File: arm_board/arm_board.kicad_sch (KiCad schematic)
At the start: 27 parts, among them J10 RJ45_LED_Shielded, Q3 BSS138, SW10 SW_Push, SW11 SW_Push, SW12 SW_Push, SW13 SW_Push, SW14 SW_Push, SW15 SW_SPDT, SW16 SW_SPDT, SW9 SW_Push

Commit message: Changed RX and TX on MCU
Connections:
- net RX+: now also U2.19 (RX+); no longer U2.20 (RX-)
- net RX-: now also U2.20 (RX-); no longer U2.19 (RX+)
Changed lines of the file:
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@@
-	(wire
-		(pts
-			(xy 67.31 167.64) (xy 71.12 167.64)
-		)
-		(stroke
-			(width 0)
-			(type default)
-		)
-	)
 	(wire
 		(pts
@@
 	(wire
 		(pts
-			(xy 67.31 170.18) (xy 71.12 170.18)
-		)
-		(stroke
-			(width 0)
-			(type default)
-		)
-	)
-	(wire
-		(pts
 			(xy 67.31 156.21) (xy 71.12 156.21)
 		)
@@
 	(wire
 		(pts
+			(xy 71.12 170.18) (xy 67.31 170.18)
+		)
+		(stroke
+			(width 0)
+			(type default)
+		)
+	)
+	(wire
+		(pts
 			(xy 33.02 168.91) (xy 43.18 168.91)
 		)
@@
 		(pts
 			(xy 229.87 137.16) (xy 238.76 137.16)
+		)
+		(stroke
+			(width 0)
+			(type default)
+		)
+	)
+	(wire
+		(pts
+			(xy 71.12 167.64) (xy 67.31 167.64)
 		)
 		(stroke
@@
 	)
 	(label "RX-"
+		(at 71.12 170.18 0)
+		(effects
+			(font
+				(size 1.27 1.27)
+			)
+			(justify left bottom)
+		)
+	)
+	(label "RX+"
 		(at 71.12 167.64 0)
 		(effects
 			(font
-				(size 1.27 1.27)
-			)
-			(justify left bottom)
-		)
-	)
-	(label "RX+"
-		(at 71.12 170.18 0)
-		(effects
-			(font

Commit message: I2C connector added
Also JST symbols added
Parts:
- removed Conn13, Conn14, Conn15, Conn16, Conn17: Molex_uF_S_03, MRDT_Connectors:MOLEX_uF_S_03_Horizontal, symbol MRDT_Connectors:Molex_uF_S_03
- removed Conn3, Conn5: Molex_uF_S_02, MRDT_Connectors:MOLEX_uF_S_02_Horizontal, symbol MRDT_Connectors:Molex_uF_S_02
- added J1: Conn_01x04_Pin, Connector_Audio:Jack_XLR_Neutrik_NC3FAAH_Horizontal, symbol Connector:Conn_01x04_Pin
- added J11, J8, J9: Conn_01x02_Pin, symbol Connector:Conn_01x02_Pin
- added J2, J5, J6, J7: Conn_01x03_Pin, symbol Connector:Conn_01x03_Pin
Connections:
- net +5V: now also J1.1 (Pin_1), J11.1 (Pin_1), J2.2 (Pin_2), J5.2 (Pin_2), J6.2 (Pin_2), J7.2 (Pin_2), J8.2 (Pin_2)
- net CAN_H: now also J9.2 (Pin_2)
- net CAN_L: now also J9.1 (Pin_1)
- net GND: now also J1.4 (Pin_4), J2.1 (Pin_1), J5.1 (Pin_1), J6.1 (Pin_1), J7.1 (Pin_1), J8.1 (Pin_1)
- net Servo_2: now also J7.3 (Pin_3)
- net Servo_3: now also J6.3 (Pin_3)
- net Servo_4: now also J5.3 (Pin_3)
- net Servo_5: now also J2.3 (Pin_3)
- net I2C_SCL: now reaches U2.28 (PB6)
- net I2C_SCL: now also J1.3 (Pin_3)
- net I2C_SDA: now reaches U2.29 (PB7)
- net I2C_SDA: now also J1.2 (Pin_2)
- net at Q3.2 (S), R7.2: now also J11.2 (Pin_2)
- no-connect marks 21 -> 19

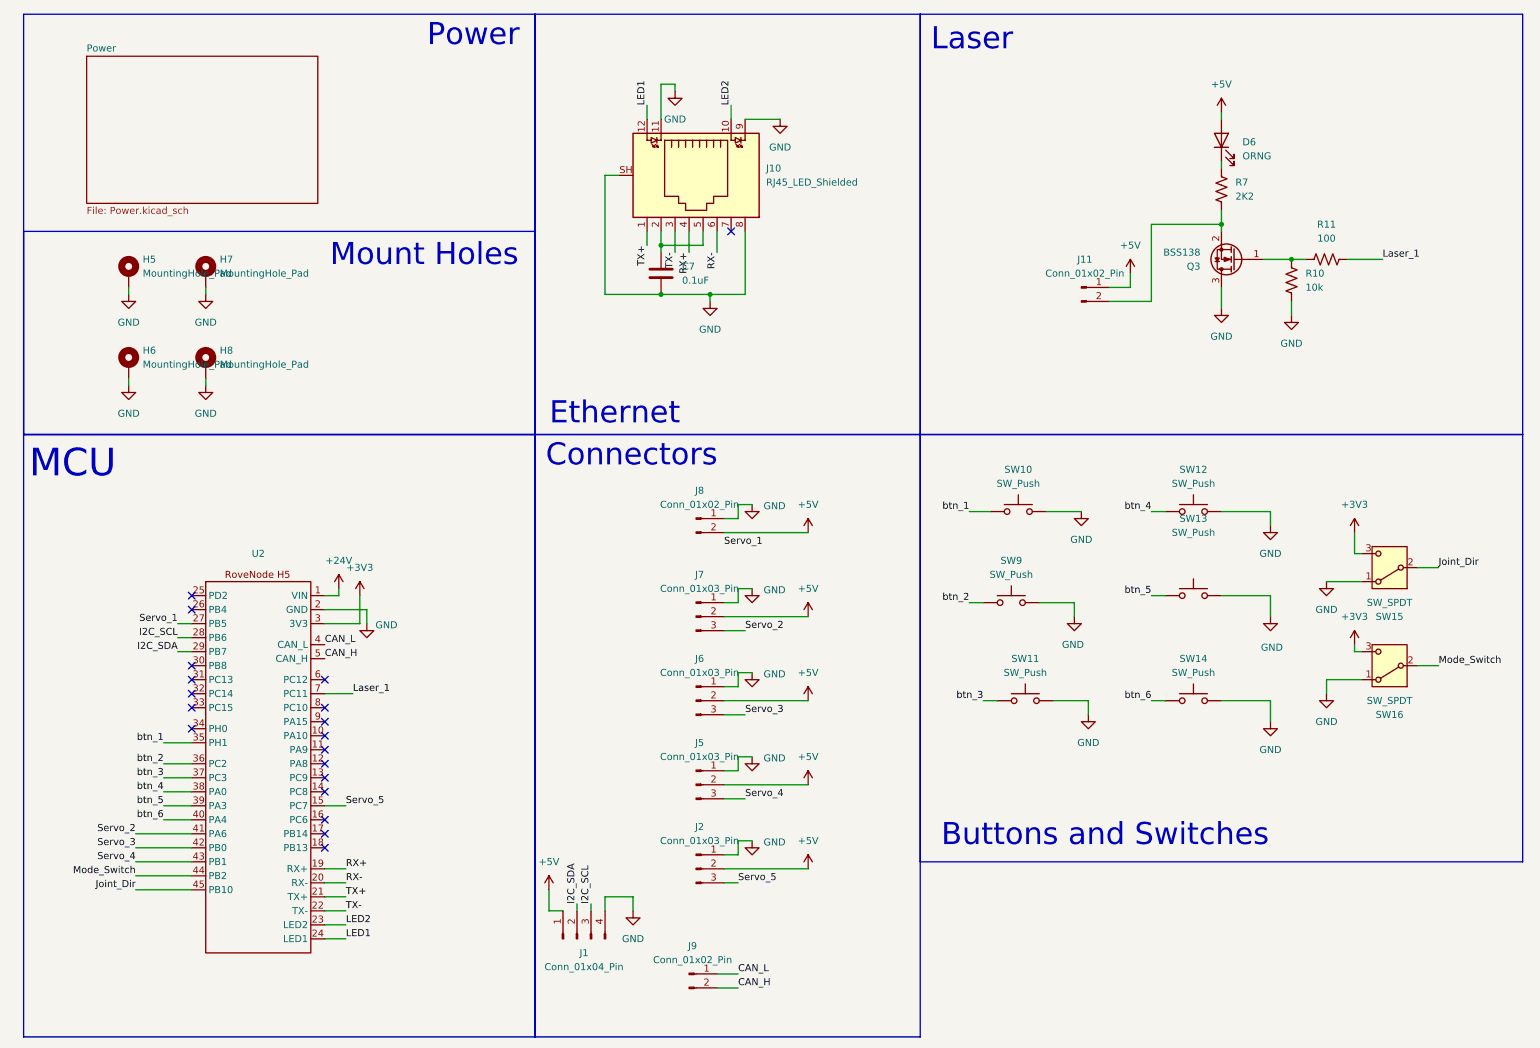
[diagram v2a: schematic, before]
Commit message: schematic meeting changes
We fixed the changes from the schematic review
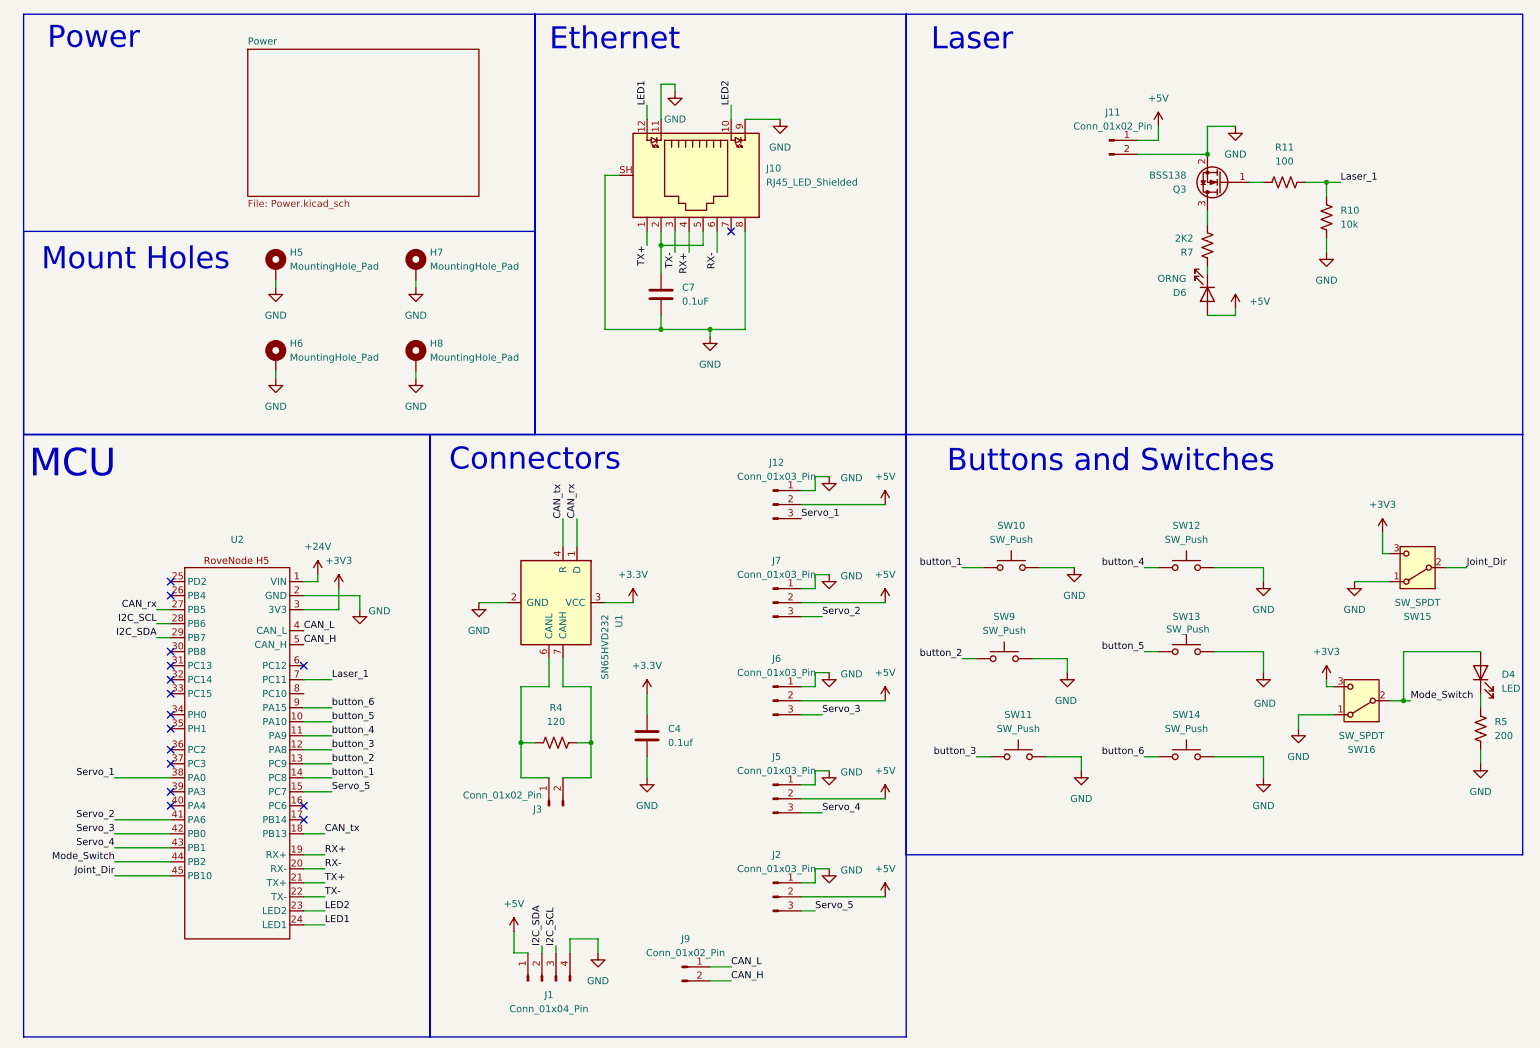
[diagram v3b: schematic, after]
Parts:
- removed J8: Conn_01x02_Pin, symbol Connector:Conn_01x02_Pin
- added C4: 0.1uf, Capacitor_SMD:C_0603_1608Metric_Pad1.08x0.95mm_HandSolder, symbol Device:C
- added D4: LED, symbol Device:LED
- added J12: Conn_01x03_Pin, Connector_JST:JST_SH_SM03B-SRSS-TB_1x03-1MP_P1.00mm_Horizontal, symbol Connector:Conn_01x03_Pin
- added J3: Conn_01x02_Pin, Oscillator:Oscillator_SMD_OCXO_ConnorWinfield_OH300, symbol Connector:Conn_01x02_Pin
- added R4: 120, Package_LCC:PLCC-84_29.3x29.3mm_P1.27mm, symbol Device:R_US
- added R5: 200, Package_LCC:PLCC-84_29.3x29.3mm_P1.27mm, symbol Device:R_US
- added U1: SN65HVD232, Package_SO:SOIC-8_3.9x4.9mm_P1.27mm, symbol Interface_CAN_LIN:SN65HVD232
- J10: footprint Connector_RJ:RJ45_Abracon_ARJP11A-MA_Horizontal -> MRDT_Connectors:RJ45_Teensy
- J11, J9: footprint (none) -> Connector_JST:JST_SH_SM02B-SRSS-TB_1x02-1MP_P1.00mm_Horizontal
- J2, J5, J6, J7: footprint (none) -> Connector_JST:JST_SH_SM03B-SRSS-TB_1x03-1MP_P1.00mm_Horizontal
- SW10, SW11, SW13, SW14, SW9: footprint Button_Switch_SMD:SW_SPST_CK_KMS2xxGP -> Button_Switch_THT:SW_Slide_SPDT_Angled_CK_OS102011MA1Q
- SW12: footprint Button_Switch_SMD:SW_SPST_CK_KMS2xxGP -> Button_Switch_SMD:SW_SPST_TL3305A
- SW15, SW16: footprint Package_SO:TSSOP-48_6.1x12.5mm_P0.5mm -> Button_Switch_THT:SW_Slide_SPDT_Angled_CK_OS102011MA1Q
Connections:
- net +5V: now also J12.2 (Pin_2)
- net GND: now also J11.2 (Pin_2), Q3.2 (S), C4.2, J12.1 (Pin_1), R5.2, U1.2 (GND); no longer Q3.3 (D)
- net Laser_1: now also R10.1
- net Mode_Switch: now also D4.2 (A)
- net Servo_1: now also U2.38 (PA0), J12.3 (Pin_3); no longer U2.27 (PB5)
- net button_5: now reaches U2.10 (PA10)
- net button_5: now also SW13.1
- net button_4: now reaches U2.11 (PA9)
- net button_4: now also SW12.1
- net button_3: now reaches U2.12 (PA8)
- net button_3: now also SW11.1
- net button_2: now reaches U2.13 (PC9)
- net button_2: now also SW9.1
- net button_1: now reaches U2.14 (PC8)
- net button_1: now also SW10.1
- net CAN_tx: now reaches U2.18 (PB13)
- net CAN_tx: now also U1.4 (R)
- net button_6: now reaches U2.9 (PA15)
- net button_6: now also SW14.1
- net at Q3.1 (G), R11.1: no longer R10.1
- net btn_1: no longer names the net of U2.35 (PH1)
- net btn_1: no longer SW10.1
- net btn_2: no longer names the net of U2.36 (PC2)
- net btn_2: no longer SW9.1
- net btn_3: no longer names the net of U2.37 (PC3)
- net btn_3: no longer SW11.1
- removed net btn_4: SW12.1, U2.38 (PA0)
- net btn_5: no longer names the net of U2.39 (PA3)
- net btn_5: no longer SW13.1
- net btn_6: no longer names the net of U2.40 (PA4)
- net btn_6: no longer SW14.1
- new net: J3.1 (Pin_1), R4.2, U1.6 (CANL)
- new net: J3.2 (Pin_2), R4.1, U1.7 (CANH)
- new net: D4.1 (K), R5.1
- new net: Q3.3 (D), R7.2
- new net +3.3V: C4.1, U1.3 (VCC)
- new net CAN_rx: U1.1 (D), U2.27 (PB5)
- no-connect marks 19 -> 16
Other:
- moved on the sheet: C7, D6, H5, H6, H7, H8, J1, J11, J2, J5, J6, J7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

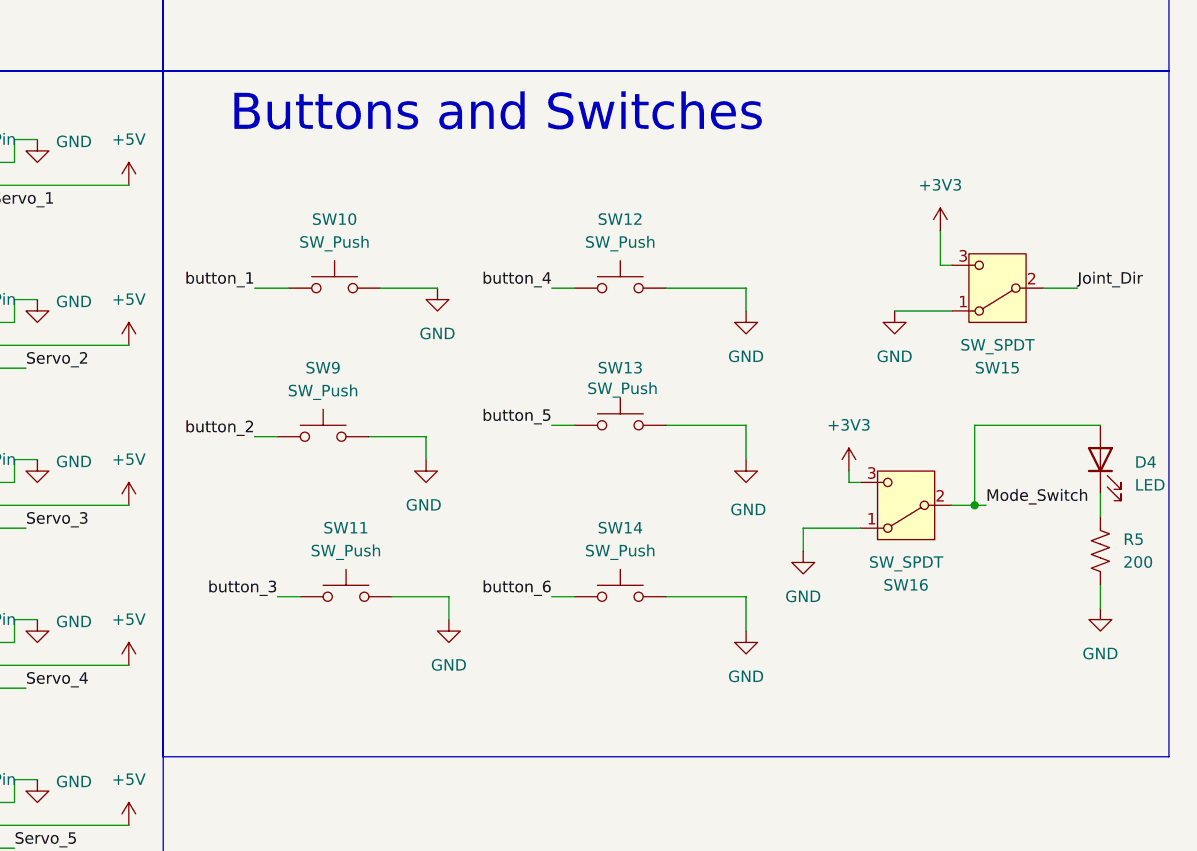
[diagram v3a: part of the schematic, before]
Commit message: footprint assigned to blue LED
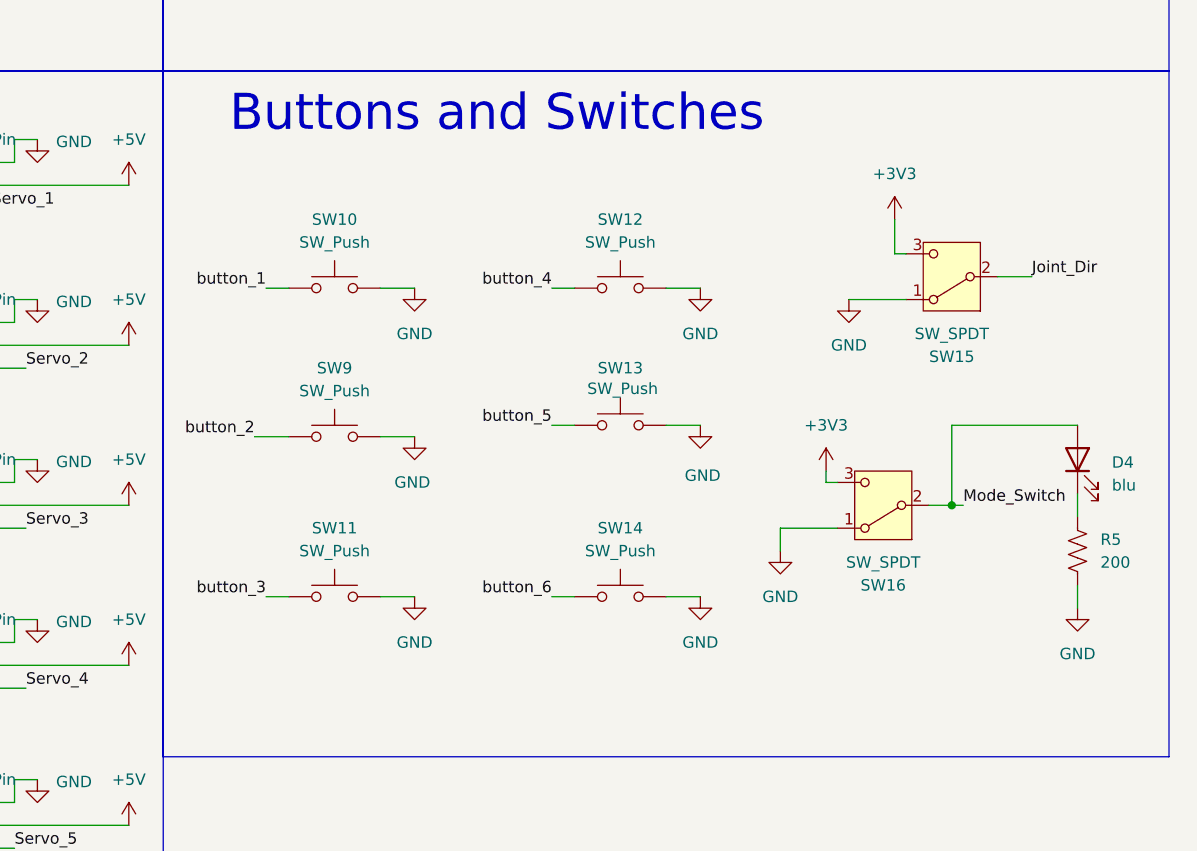
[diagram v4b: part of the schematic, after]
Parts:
- D4: value LED -> blu
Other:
- moved on the sheet: D4, R5, SW11, SW15, SW16, SW9
